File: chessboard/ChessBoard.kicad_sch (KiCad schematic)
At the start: 1 part

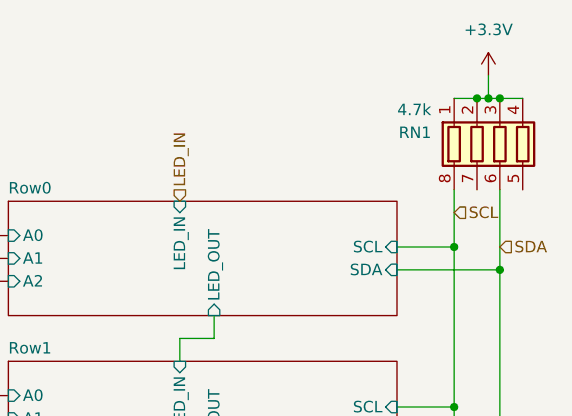
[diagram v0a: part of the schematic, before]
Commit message: add some power logic, split chessboard and control board
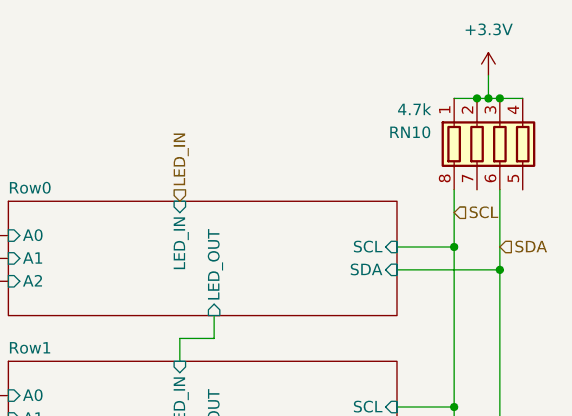
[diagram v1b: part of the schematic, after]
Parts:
- renumbered RN1 to RN10
